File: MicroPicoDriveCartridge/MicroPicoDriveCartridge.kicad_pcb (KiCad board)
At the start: 2 copper layers, 40.3 x 35 mm, 9 parts, among them J1 Edge Connector, J2 0.96 IPS ST7735S, J3 K1..K4, J4 DM3D-SF

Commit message: Stagger cartridge edge fingers for hot-swap mating order
GND (pin 3) and the GND-tied UI_DETECT (pin 14) keep the full 8 mm
length and mate first, +3V3 is retracted 1 mm, and all signal fingers
are retracted 1.75 mm so they mate last and break first. Gerbers and
iBOM regenerated; the Edge library footprint is synced with the board.
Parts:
- J1: footprint CartridgeComponents:Edge -> My Footprint Library:MicroPicoDrive Cartridge Edge
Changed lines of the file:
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@@
 		)
 	)
-	(footprint "CartridgeComponents:Edge"
+	(footprint "My Footprint Library:MicroPicoDrive Cartridge Edge"
 		(layer "F.Cu")
 		(at 142.725 67.975)
@@
 			(unlocked yes)
 			(layer "F.SilkS")
-			(hide yes)
 			(effects
 				(font
@@
 			(unlocked yes)
 			(layer "F.Fab")
-			(hide yes)
 			(effects
 				(font
@@
 				(font
 					(size 1.27 1.27)
-				)
-			)
-		)
-		(property "Field4" "${REFERENCE}"
-			(at -10.5664 -5.9944 0)
-			(unlocked yes)
-			(layer "F.Fab")
-			(hide yes)
-			(effects
-				(font
-					(size 1 1)
-					(thickness 0.15)
 				)
 			)
@@
 			(layer "Edge.Cuts")
 		)
+		(fp_text user "${REFERENCE}"
+			(at -10.5664 -5.9944 0)
+			(unlocked yes)
+			(layer "F.Fab")
+			(effects
+				(font
+					(size 1 1)
+					(thickness 0.15)
+				)
+			)
+		)
 		(pad "1" smd roundrect
-			(at -8.89 0)
-			(size 2 8)
+			(at -8.89 0.5)
+			(size 2 7)
 			(layers "F.Cu" "F.Mask" "F.Paste")
 			(roundrect_rratio 0.25)
@@
 		)
 		(pad "2" smd roundrect
-			(at -8.89 0)
-			(size 2 8)
+			(at -8.89 0.875)
+			(size 2 6.25)
 			(layers "B.Cu" "B.Mask" "B.Paste")
 			(roundrect_rratio 0.25)
@@
 		)
 		(pad "4" smd roundrect
-			(at -6.35 0)
-			(size 2 8)
+			(at -6.35 0.875)
+			(size 2 6.25)
 			(layers "B.Cu" "B.Mask" "B.Paste")
 			(roundrect_rratio 0.25)
@@
 		)
 		(pad "5" smd roundrect
-			(at -3.81 0)
-			(size 2 8)
+			(at -3.81 0.875)
+			(size 2 6.25)
 			(layers "F.Cu" "F.Mask" "F.Paste")
 			(roundrect_rratio 0.25)
@@
 		)
 		(pad "6" smd roundrect
-			(at -3.81 0)
-			(size 2 8)
-			(layers "B.Cu" "B.Mask" "B.Paste")
+			(at -3.81 0.875)
+			(size 2 6.25)
+			(layers "B.Cu" "B.Mask" "B.SilkS" "B.Paste")
 			(roundrect_rratio 0.25)
 			(net "/UI_SD_CS")
@@
 		)
 		(pad "7" smd roundrect
-			(at -1.27 0)
-			(size 2 8)
+			(at -1.27 0.875)
+			(size 2 6.25)
 			(layers "F.Cu" "F.Mask" "F.Paste")
 			(roundrect_rratio 0.25)
@@
 		)
 		(pad "8" smd roundrect
-			(at -1.27 0)
-			(size 2 8)
+			(at -1.27 0.875)
+			(size 2 6.25)
 			(layers "B.Cu" "B.Mask" "B.Paste")
 			(roundrect_rratio 0.25)
@@
 		)
 		(pad "9" smd roundrect
-			(at 1.27 0)
-			(size 2 8)
+			(at 1.27 0.875)
+			(size 2 6.25)
 			(layers "F.Cu" "F.Mask" "F.Paste")
 			(roundrect_rratio 0.25)
@@
 		)
 		(pad "10" smd roundrect
-			(at 1.27 0)
-			(size 2 8)
+			(at 1.27 0.875)
+			(size 2 6.25)
 			(layers "B.Cu" "B.Mask" "B.Paste")
 			(roundrect_rratio 0.25)
@@
 		)
 		(pad "11" smd roundrect
-			(at 3.81 0)
-			(size 2 8)
+			(at 3.81 0.875)
+			(size 2 6.25)
 			(layers "F.Cu" "F.Mask" "F.Paste")
 			(roundrect_rratio 0.25)
@@
 		)
 		(pad "12" smd roundrect
-			(at 3.81 0)
-			(size 2 8)
+			(at 3.81 0.875)
+			(size 2 6.25)
 			(layers "B.Cu" "B.Mask" "B.Paste")
 			(roundrect_rratio 0.25)
@@
 		)
 		(pad "13" smd roundrect
-			(at 6.35 0)
-			(size 2 8)
+			(at 6.35 0.875)
+			(size 2 6.25)
 			(layers "F.Cu" "F.Mask" "F.Paste")
 			(roundrect_rratio 0.25)
@@
 		)
 		(pad "15" smd roundrect
-			(at 8.89 0)
-			(size 2 8)
+			(at 8.89 0.875)
+			(size 2 6.25)
 			(layers "F.Cu" "F.Mask" "F.Paste")
 			(roundrect_rratio 0.25)
@@
 		)
 		(pad "16" smd roundrect
-			(at 8.89 0)
-			(size 2 8)
-			(layers "B.Cu" "B.Mask" "B.Paste")
-			(roundrect_rratio 0.25)
+			(at 8.89 0.875)
+			(size 2 6.25)
+			(layers "B.Cu" "B.Mask" "B.Paste")
+			(roundrect_rratio 0.25)

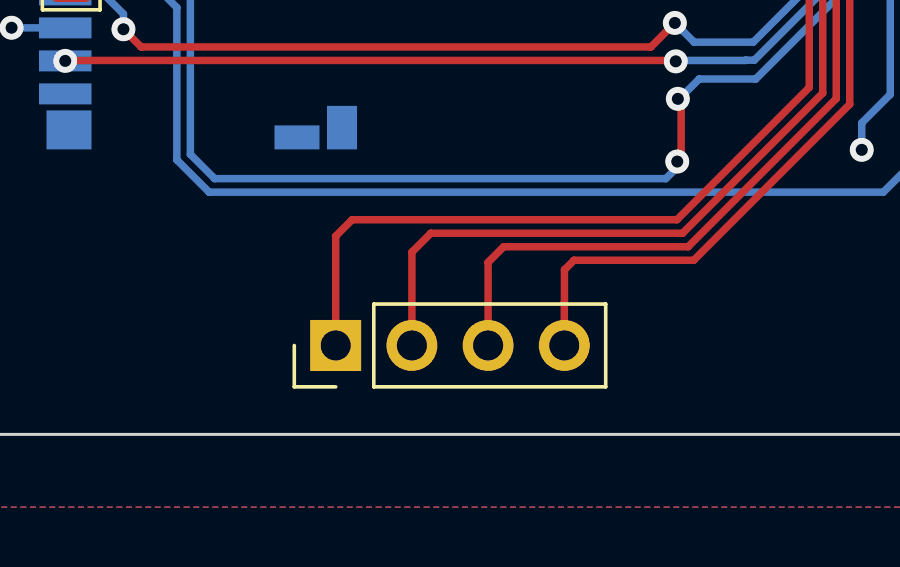
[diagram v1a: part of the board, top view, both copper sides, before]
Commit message: Add mainboard silkscreen labels and cartridge copper zone
Mainboard gains front-silkscreen labelling (KiBuzzard label and text
items); the cartridge PCB gets a new copper pour. Gerbers re-exported
for both boards.
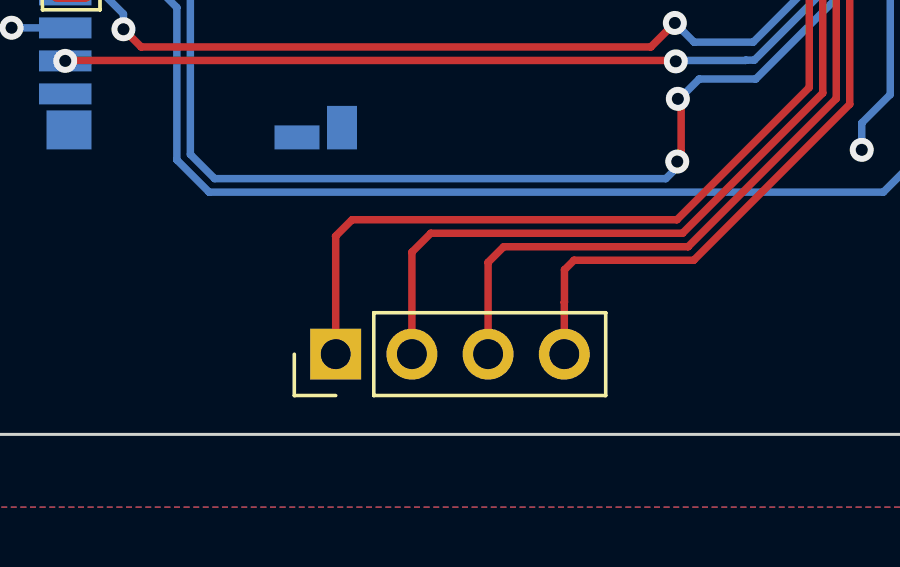
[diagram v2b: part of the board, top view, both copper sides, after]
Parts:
- moved J3 0.29 mm to (138.9, 105.7)
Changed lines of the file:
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@@
 	(footprint "Connector_PinHeader_2.54mm:PinHeader_1x04_P2.54mm_Vertical"
 		(layer "F.Cu")
-		(at 138.915001 105.41 90)
+		(at 138.915001 105.7 90)
 		(descr "Through hole straight pin header, 1x04, 2.54mm pitch, single row")
 		(tags "Through hole pin header THT 1x04 2.54mm single row")
@@
 	)
 	(segment
+		(start 143.995 67.975)
+		(end 143.995 74.78)
+		(width 0.25)
+		(layer "F.Cu")
+		(net "/UI_BTN_BACK")
+	)
+	(segment
+		(start 143.995 74.78)
+		(end 144.915 75.7)
+		(width 0.25)
+		(layer "F.Cu")
+		(net "/UI_BTN_BACK")
+	)
+	(segment
+		(start 144.915 75.7)
+		(end 154.3 75.7)
+		(width 0.25)
+		(layer "F.Cu")
+		(net "/UI_BTN_BACK")
+	)
+	(segment
+		(start 154.7 76.1)
+		(end 154.7 96.81)
+		(width 0.25)
+		(layer "F.Cu")
+		(net "/UI_BTN_BACK")
+	)
+	(segment
+		(start 138.91 101.77)
+		(end 138.915001 101.775001)
+		(width 0.25)
+		(layer "F.Cu")
+		(net "/UI_BTN_BACK")
+	)
+	(segment
+		(start 138.915001 101.775001)
+		(end 138.915001 105.7)
+		(width 0.25)
+		(layer "F.Cu")
+		(net "/UI_BTN_BACK")
+	)
+	(segment
+		(start 154.3 75.7)
+		(end 154.7 76.1)
+		(width 0.25)
+		(layer "F.Cu")
+		(net "/UI_BTN_BACK")
+	)
+	(segment
 		(start 139.46 101.22)
 		(end 138.91 101.77)
@@
 		(start 150.29 101.22)
 		(end 139.46 101.22)
-		(width 0.25)
-		(layer "F.Cu")
-		(net "/UI_BTN_BACK")
-	)
-	(segment
-		(start 143.995 67.975)
-		(end 143.995 74.78)
-		(width 0.25)
-		(layer "F.Cu")
-		(net "/UI_BTN_BACK")
-	)
-	(segment
-		(start 154.7 76.1)
-		(end 154.7 96.81)
-		(width 0.25)
-		(layer "F.Cu")
-		(net "/UI_BTN_BACK")
-	)
-	(segment
-		(start 154.3 75.7)
-		(end 154.7 76.1)
-		(width 0.25)
-		(layer "F.Cu")
-		(net "/UI_BTN_BACK")
-	)
-	(segment
-		(start 138.91 101.77)
-		(end 138.915001 101.775001)
-		(width 0.25)
-		(layer "F.Cu")
-		(net "/UI_BTN_BACK")
-	)
-	(segment
-		(start 138.915001 101.775001)
-		(end 138.915001 105.41)
-		(width 0.25)
-		(layer "F.Cu")
-		(net "/UI_BTN_BACK")
-	)
-	(segment
-		(start 143.995 74.78)
-		(end 144.915 75.7)
-		(width 0.25)
-		(layer "F.Cu")
-		(net "/UI_BTN_BACK")
-	)
-	(segment
-		(start 144.915 75.7)
-		(end 154.3 75.7)
 		(width 0.25)
 		(layer "F.Cu")
@@
 	)
 	(segment
+		(start 150.476396 101.67)
+		(end 142.086 101.67)
+		(width 0.25)
+		(layer "F.Cu")
+		(net "/UI_BTN_NEXT")
+	)
+	(segment
+		(start 147.386 75.25)
+		(end 154.486396 75.25)
+		(width 0.25)
+		(layer "F.Cu")
+		(net "/UI_BTN_NEXT")
+	)
+	(segment
+		(start 142.086 101.67)
+		(end 141.455001 102.300999)
+		(width 0.25)
+		(layer "F.Cu")
+		(net "/UI_BTN_NEXT")
+	)
+	(segment
+		(start 146.535 74.399)
+		(end 147.386 75.25)
+		(width 0.25)
+		(layer "F.Cu")
+		(net "/UI_BTN_NEXT")
+	)
+	(segment
+		(start 141.455001 102.300999)
+		(end 141.455001 105.7)
+		(width 0.25)
+		(layer "F.Cu")
+		(net "/UI_BTN_NEXT")
+	)
+	(segment
+		(start 146.535 67.975)
+		(end 146.535 74.399)
+		(width 0.25)
+		(layer "F.Cu")
+		(net "/UI_BTN_NEXT")
+	)
+	(segment
+		(start 155.15 96.996396)
+		(end 150.476396 101.67)
+		(width 0.25)
+		(layer "F.Cu")
+		(net "/UI_BTN_NEXT")
+	)
+	(segment
 		(start 154.486396 75.25)
 		(end 155.15 75.913604)
-		(width 0.25)
-		(layer "F.Cu")
-		(net "/UI_BTN_NEXT")
-	)
-	(segment
-		(start 146.535 74.399)
-		(end 147.386 75.25)
-		(width 0.25)
-		(layer "F.Cu")
-		(net "/UI_BTN_NEXT")
-	)
-	(segment
-		(start 155.15 96.996396)
-		(end 150.476396 101.67)
-		(width 0.25)
-		(layer "F.Cu")
-		(net "/UI_BTN_NEXT")
-	)
-	(segment
-		(start 142.086 101.67)
-		(end 141.455001 102.300999)
-		(width 0.25)
-		(layer "F.Cu")
-		(net "/UI_BTN_NEXT")
-	)
-	(segment
-		(start 150.476396 101.67)
-		(end 142.086 101.67)
-		(width 0.25)
-		(layer "F.Cu")
-		(net "/UI_BTN_NEXT")
-	)
-	(segment
-		(start 147.386 75.25)
-		(end 154.486396 75.25)
-		(width 0.25)
-		(layer "F.Cu")
-		(net "/UI_BTN_NEXT")
-	)
-	(segment
-		(start 141.455001 102.300999)
-		(end 141.455001 105.41)
-		(width 0.25)
-		(layer "F.Cu")
-		(net "/UI_BTN_NEXT")
-	)
-	(segment
-		(start 146.535 67.975)
-		(end 146.535 74.399)
 		(width 0.25)
 		(layer "F.Cu")
@@
 	)
 	(segment
+		(start 150.662792 102.12)
+		(end 144.514 102.12)
+		(width 0.25)
+		(layer "F.Cu")
+		(net "/UI_BTN_SELECT")
+	)
+	(segment
+		(start 155.6 97.182792)
+		(end 150.662792 102.12)
+		(width 0.25)
+		(layer "F.Cu")
+		(net "/UI_BTN_SELECT")
+	)
+	(segment
+		(start 143.995 102.639)
+		(end 143.995 105.7)
+		(width 0.25)
+		(layer "F.Cu")
+		(net "/UI_BTN_SELECT")
+	)
+	(segment
+		(start 149.075 74.175)
+		(end 149.7 74.8)
+		(width 0.25)
+		(layer "F.Cu")
+		(net "/UI_BTN_SELECT")
+	)
+	(segment
+		(start 149.7 74.8)
+		(end 154.672792 74.8)
+		(width 0.25)
+		(layer "F.Cu")
+		(net "/UI_BTN_SELECT")
+	)
+	(segment
+		(start 155.6 75.727208)
+		(end 155.6 97.182792)
+		(width 0.25)
+		(layer "F.Cu")
+		(net "/UI_BTN_SELECT")
+	)
+	(segment
+		(start 154.672792 74.8)
+		(end 155.6 75.727208)
+		(width 0.25)
+		(layer "F.Cu")
+		(net "/UI_BTN_SELECT")
+	)
+	(segment
+		(start 149.075 67.975)
+		(end 149.075 74.175)
+		(width 0.25)
+		(layer "F.Cu")
+		(net "/UI_BTN_SELECT")
+	)
+	(segment
 		(start 144.514 102.12)
 		(end 143.995 102.639)
@@
 	)
 	(segment
-		(start 154.672792 74.8)
-		(end 155.6 75.727208)
-		(width 0.25)
-		(layer "F.Cu")
-		(net "/UI_BTN_SELECT")
-	)
-	(segment
-		(start 149.075 67.975)
-		(end 149.075 74.175)
-		(width 0.25)
-		(layer "F.Cu")
-		(net "/UI_BTN_SELECT")
-	)
-	(segment
-		(start 143.995 102.639)
-		(end 143.995 105.41)
-		(width 0.25)
-		(layer "F.Cu")
-		(net "/UI_BTN_SELECT")
-	)
-	(segment
-		(start 155.6 97.182792)
-		(end 150.662792 102.12)
-		(width 0.25)
-		(layer "F.Cu")
-		(net "/UI_BTN_SELECT")
-	)
-	(segment
-		(start 150.662792 102.12)
-		(end 144.514 102.12)
-		(width 0.25)
-		(layer "F.Cu")
-		(net "/UI_BTN_SELECT")
-	)
-	(segment
-		(start 149.7 74.8)
-		(end 154.672792 74.8)
-		(width 0.25)
-		(layer "F.Cu")
-		(net "/UI_BTN_SELECT")
-	)
-	(segment
-		(start 149.075 74.175)
-		(end 149.7 74.8)
-		(width 0.25)
-		(layer "F.Cu")
-		(net "/UI_BTN_SELECT")
-	)
-	(segment
-		(start 155.6 75.727208)
-		(end 155.6 97.182792)
-		(width 0.25)
-		(layer "F.Cu")
-		(net "/UI_BTN_SELECT")
+		(start 151.85 74.35)
+		(end 154.859188 74.35)
+		(width 0.25)
+		(layer "F.Cu")
+		(net "/UI_BTN_K4")
+	)
+	(segment
+		(start 146.858 102.57)
+		(end 146.54 102.888)
+		(width 0.25)
+		(layer "F.Cu")
+		(net "/UI_BTN_K4")
+	)
+	(segment
+		(start 146.54 102.888)
+		(end 146.54 103.97)
+		(width 0.25)
+		(layer "F.Cu")
+		(net "/UI_BTN_K4")
+	)
+	(segment
+		(start 156.05 75.540812)
+		(end 156.05 97.369188)
+		(width 0.25)
+		(layer "F.Cu")
+		(net "/UI_BTN_K4")
+	)
+	(segment
+		(start 151.615 74.115)
+		(end 151.85 74.35)
+		(width 0.25)
+		(layer "F.Cu")
+		(net "/UI_BTN_K4")
+	)
+	(segment
+		(start 151.615 67.975)
+		(end 151.615 74.115)
+		(width 0.25)
+		(layer "F.Cu")
+		(net "/UI_BTN_K4")
+	)
+	(segment
+		(start 156.05 97.369188)
+		(end 150.849188 102.57)
+		(width 0.25)
+		(layer "F.Cu")
+		(net "/UI_BTN_K4")
 	)
 	(segment
@@
 	)
 	(segment
-		(start 156.05 97.369188)
-		(end 150.849188 102.57)
-		(width 0.25)
-		(layer "F.Cu")
-		(net "/UI_BTN_K4")
-	)
-	(segment
-		(start 151.85 74.35)
-		(end 154.859188 74.35)
+		(start 154.859188 74.35)
+		(end 156.05 75.540812)
 		(width 0.25)
 		(layer "F.Cu")
@@
 	)
 	(segment
-		(start 154.859188 74.35)
-		(end 156.05 75.540812)
-		(width 0.25)
-		(layer "F.Cu")
-		(net "/UI_BTN_K4")
-	)
-	(segment
-		(start 151.615 74.115)
-		(end 151.85 74.35)
-		(width 0.25)
-		(layer "F.Cu")
-		(net "/UI_BTN_K4")
-	)
-	(segment
 		(start 146.535001 103.974999)
-		(end 146.535001 105.41)
-		(width 0.25)
-		(layer "F.Cu")
-		(net "/UI_BTN_K4")
-	)
-	(segment
-		(start 156.05 75.540812)
-		(end 156.05 97.369188)
-		(width 0.25)
-		(layer "F.Cu")
-		(net "/UI_BTN_K4")
-	)
-	(segment
-		(start 151.615 67.975)
-		(end 151.615 74.115)
-		(width 0.25)
-		(layer "F.Cu")
-		(net "/UI_BTN_K4")
-	)
-	(segment
-		(start 146.858 102.57)
-		(end 146.54 102.888)
-		(width 0.25)
-		(layer "F.Cu")
-		(net "/UI_BTN_K4")
-	)
-	(segment
-		(start 146.54 102.888)
-		(end 146.54 103.97)
+		(end 146.535001 105.7)
 		(width 0.25)
 		(layer "F.Cu")
@@
 		)
 	)
+	(zone
+		(layers "*.Mask")
+		(hatch edge 0.5)
+		(connect_pads
+			(clearance 0)
+		)
+		(min_thickness 0.25)
+		(fill yes
+			(thermal_gap 0.5)
+			(thermal_bridge_width 0.5)
+			(island_removal_mode 0)
+		)
+		(polygon
+			(pts
+				(xy 130 63) (xy 155 63) (xy 155 71) (xy 130 71)
+			)
+		)
+	)
 	(group ""
-		(members "834521bf-e89d-4272-bca4-b07a518d34df" "e5bb18b1-441d-4a30-9515-19227b7fc824")
-	)
-	(group ""
